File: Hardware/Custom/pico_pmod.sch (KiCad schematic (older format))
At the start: 31 parts, among them J1 Conn_02x06_Odd_Even, J2 Conn_02x06_Odd_Even, J3 Conn_02x06_Odd_Even, J4 USB_C_Receptacle_USB2.0, SW1 SW_Push, SW2 SW_Push, U1 RP2040, U2 W25Q128JVS, U3 NCP1117-3.3_SOT223, Y1 12MHz

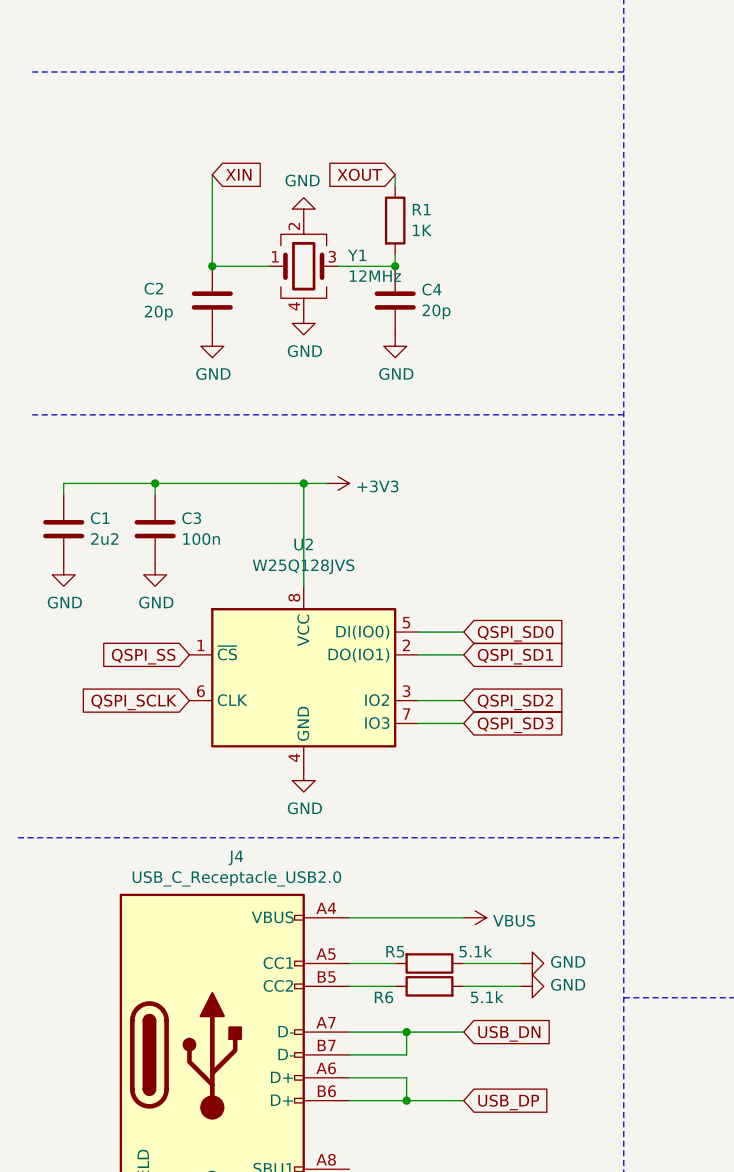
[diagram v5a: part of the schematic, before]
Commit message: Add the USB resitors and route power supply
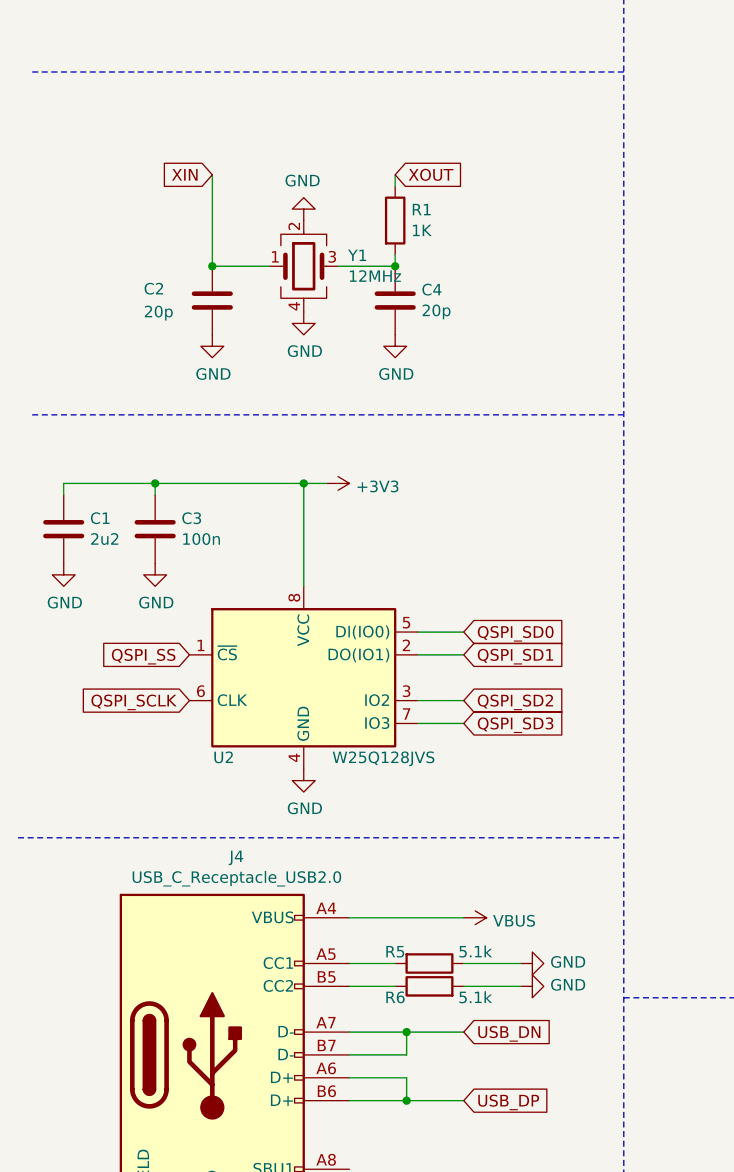
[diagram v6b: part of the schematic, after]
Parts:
- J?: footprint (none) -> Connector_PinHeader_2.54mm:PinHeader_1x04_P2.54mm_Vertical
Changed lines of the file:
@@
 	1    0    0    -1
 $EndComp
-Text GLabel 1300 2700 2    51   Input ~ 0
+Text GLabel 1300 2700 0    51   Input ~ 0
 XIN
-Text GLabel 2100 2700 0    51   Input ~ 0
+Text GLabel 2100 2700 2    51   Input ~ 0
 XOUT
 Wire Wire Line
@@
 U 1 1 60FC35B9
 P 2250 6250
-F 0 "R6" V 2200 6450 50  0000 C CNN
-F 1 "5.1k" V 2200 6000 50  0000 C CNN
+F 0 "R6" V 2200 6400 50  0000 C CNN
+F 1 "5.1k" V 2200 6050 50  0000 C CNN
 F 2 "Resistor_SMD:R_0603_1608Metric" V 2180 6250 50  0001 C CNN
 F 3 "~" H 2250 6250 50  0001 C CNN
@@
 U 1 1 60EF4959
 P 1700 4900
-F 0 "U2" H 1700 5481 50  0000 C CNN
-F 1 "W25Q128JVS" H 1700 5390 50  0000 C CNN
+F 0 "U2" H 1350 4550 50  0000 C CNN
+F 1 "W25Q128JVS" H 2050 4550 50  0000 C CNN
 F 2 "Package_SO:SOIC-8_5.23x5.23mm_P1.27mm" H 1700 4900 50  0001 C CNN
 F 3 "http://www.winbond.com/resource-files/w25q128jv_dtr%20revc%2003272018%20plus.pdf" H 1700 4900 50  0001 C CNN
@@
 F 0 "J?" H 2130 1392 50  0000 L CNN
 F 1 "Conn_01x04" H 2130 1301 50  0000 L CNN
-F 2 "" H 2050 1400 50  0001 C CNN
+F 2 "Connector_PinHeader_2.54mm:PinHeader_1x04_P2.54mm_Vertical" H 2050 1400 50  0001 C CNN
 F 3 "~" H 2050 1400 50  0001 C CNN
 	1    2050 1400

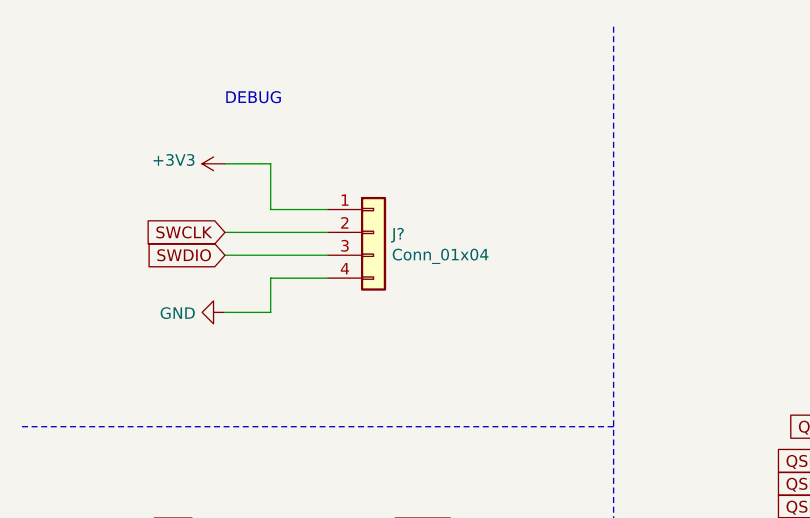
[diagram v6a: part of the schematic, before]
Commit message: Add the debug port footprint
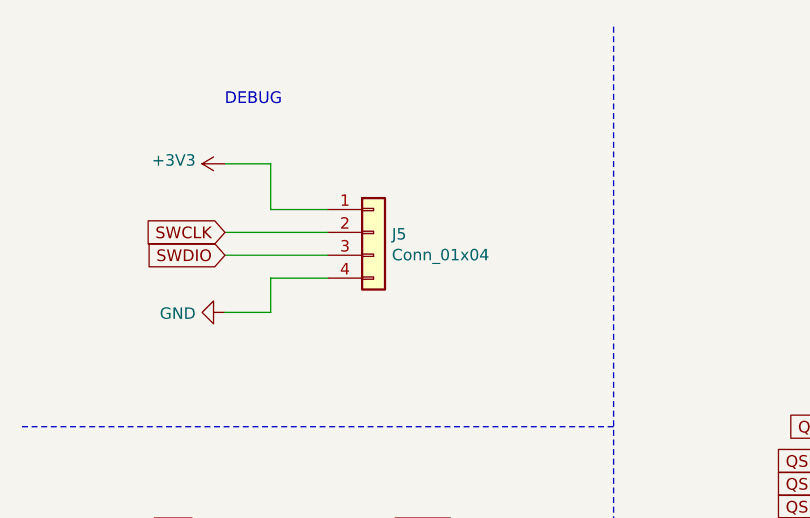
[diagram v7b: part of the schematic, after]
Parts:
- gave numbers to parts that had none: 1
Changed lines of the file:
@@
 Connection ~ 8600 5600
 $Comp
-L power:+3V3 #PWR?
+L power:+3V3 #PWR0142
 U 1 1 60FE16A7
 P 1400 1100
-F 0 "#PWR?" H 1400 950 50  0001 C CNN
+F 0 "#PWR0142" H 1400 950 50  0001 C CNN
 F 1 "+3V3" V 1415 1228 50  0000 L CNN
 F 2 "" H 1400 1100 50  0001 C CNN
@@
 $EndComp
 $Comp
-L Connector_Generic:Conn_01x04 J?
+L Connector_Generic:Conn_01x04 J5
 U 1 1 60FE2381
 P 2050 1400
-F 0 "J?" H 2130 1392 50  0000 L CNN
+F 0 "J5" H 2130 1392 50  0000 L CNN
 F 1 "Conn_01x04" H 2130 1301 50  0000 L CNN
 F 2 "Connector_PinHeader_2.54mm:PinHeader_1x04_P2.54mm_Vertical" H 2050 1400 50  0001 C CNN

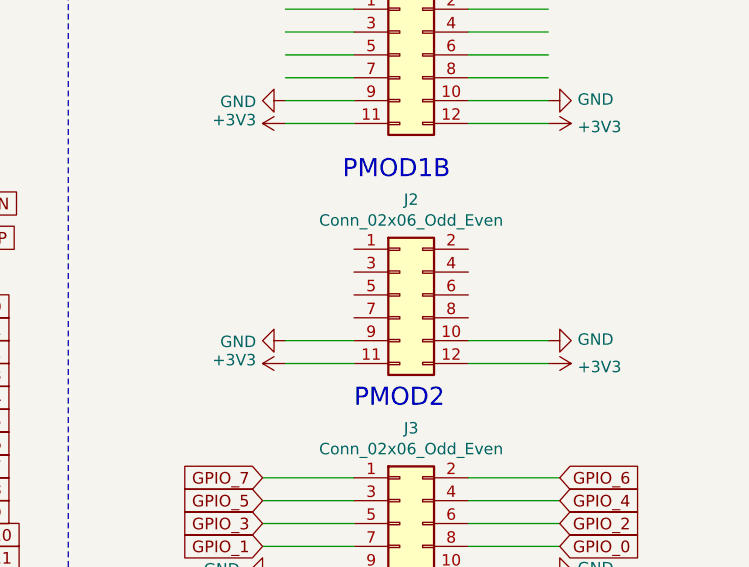
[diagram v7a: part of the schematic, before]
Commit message: PCB layout for PMOD1B and PMOD2
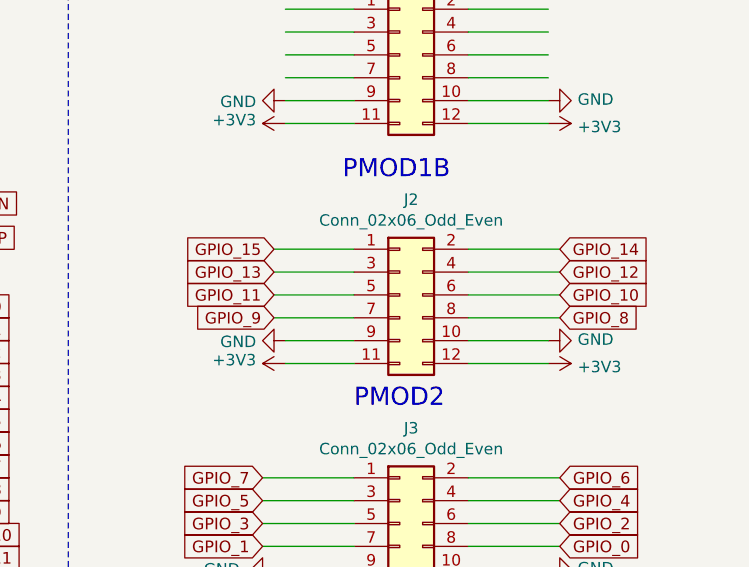
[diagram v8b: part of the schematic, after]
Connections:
- wire segments 156 -> 164
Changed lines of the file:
@@
 Wire Notes Line
 	3100 500  3100 7800
+Text GLabel 10450 2250 2    50   Input ~ 0
+GPIO_8
+Text GLabel 10450 2150 2    50   Input ~ 0
+GPIO_10
+Text GLabel 10450 2050 2    50   Input ~ 0
+GPIO_12
+Text GLabel 10450 1950 2    50   Input ~ 0
+GPIO_14
+Wire Wire Line
+	10450 2250 10050 2250
+Wire Wire Line
+	10050 2150 10450 2150
+Wire Wire Line
+	10450 2050 10050 2050
+Wire Wire Line
+	10050 1950 10450 1950
+Text GLabel 9200 2250 0    50   Input ~ 0
+GPIO_9
+Text GLabel 9200 2150 0    50   Input ~ 0
+GPIO_11
+Text GLabel 9200 2050 0    50   Input ~ 0
+GPIO_13
+Text GLabel 9200 1950 0    50   Input ~ 0
+GPIO_15
+Wire Wire Line
+	9200 2250 9550 2250
+Wire Wire Line
+	9550 2150 9200 2150
+Wire Wire Line
+	9200 2050 9550 2050
+Wire Wire Line
+	9550 1950 9200 1950
 $EndSCHEMATC
